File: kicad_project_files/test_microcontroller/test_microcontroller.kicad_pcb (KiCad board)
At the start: 2 copper layers, 60 x 100 mm, 40 parts, among them J1 USB_C_Receptacle_USB2.0, SW1 SW_Push, SW2 SW_Push, SW3 SW_Push, SW4 SW_Push, SW5 SW_Push, SW6 SW_Push, SW7 SW_Push, SW8 SW_Push, SW9 SW_Push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

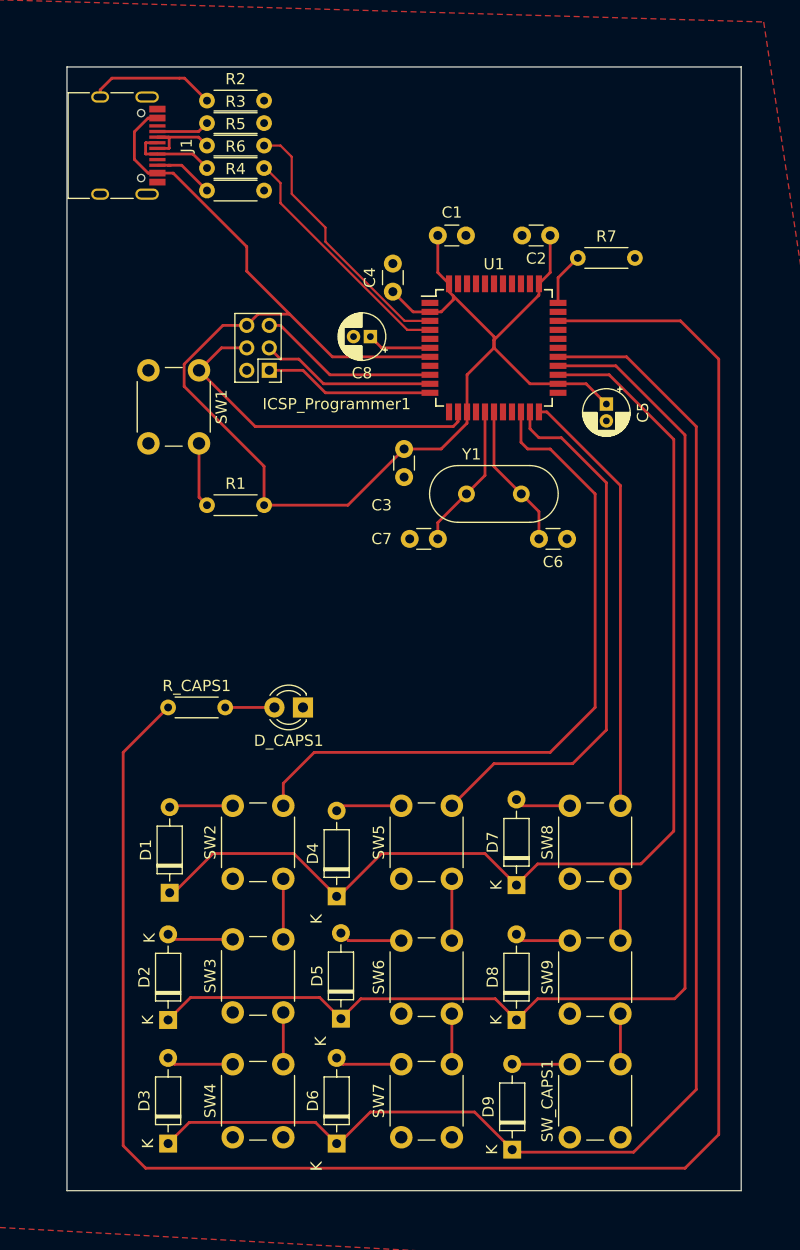
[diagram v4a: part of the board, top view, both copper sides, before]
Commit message: make tracks larger
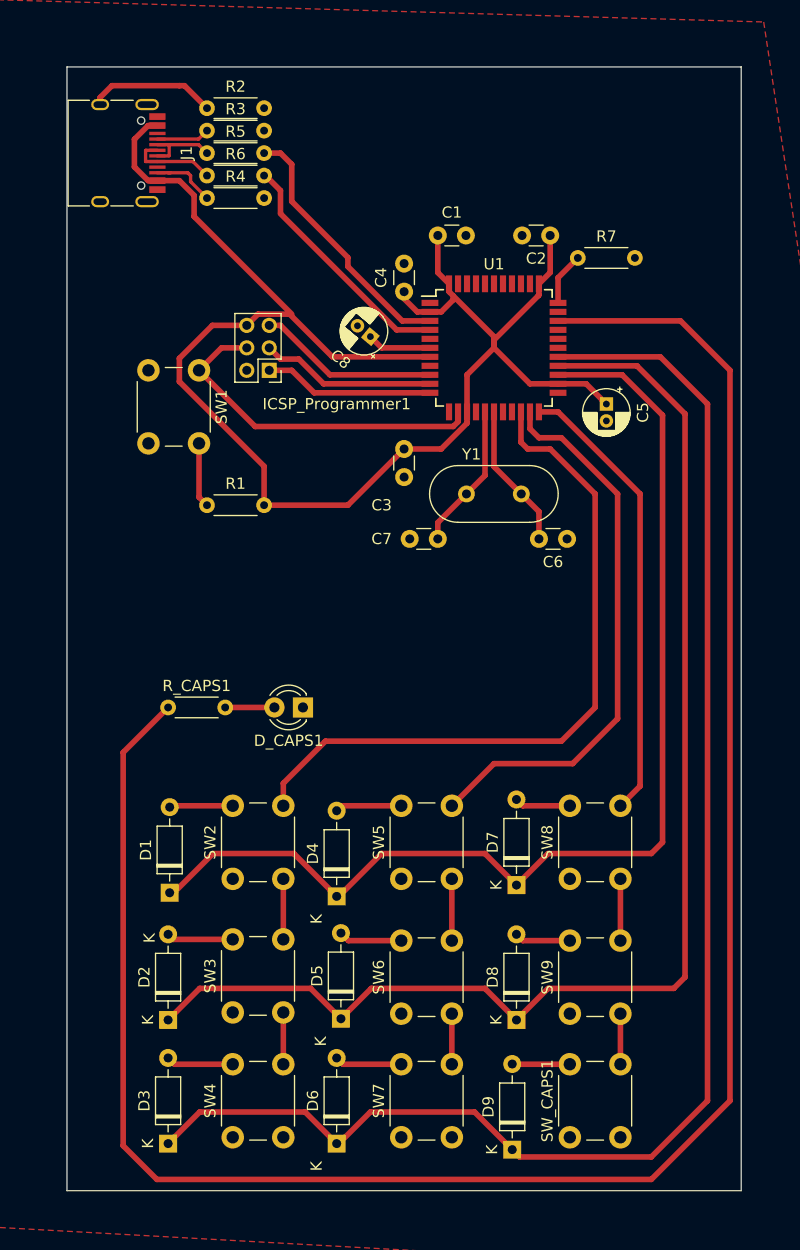
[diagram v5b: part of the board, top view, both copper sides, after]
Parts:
- moved C4 1.00 mm to (59.0, 40.0)
- moved J1 0.67 mm to (33.0, 27.7)
- moved R2 0.67 mm to (41.5, 23.7)
- moved R3 0.67 mm to (41.5, 25.7)
- moved R4 0.67 mm to (41.5, 31.7)
- moved R5 0.67 mm to (41.5, 27.7)
- moved R6 0.67 mm to (41.5, 29.7)
- turned C8 to 140 degrees
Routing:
- net ROW3: track 127.4 -> 132.3 mm
- net COL3: track 48.5 -> 50.5 mm
- net ROW2: track 113.4 -> 115.3 mm
- net COL2: track 58.8 -> 59.7 mm
- net D-: track 23.9 -> 23.3 mm

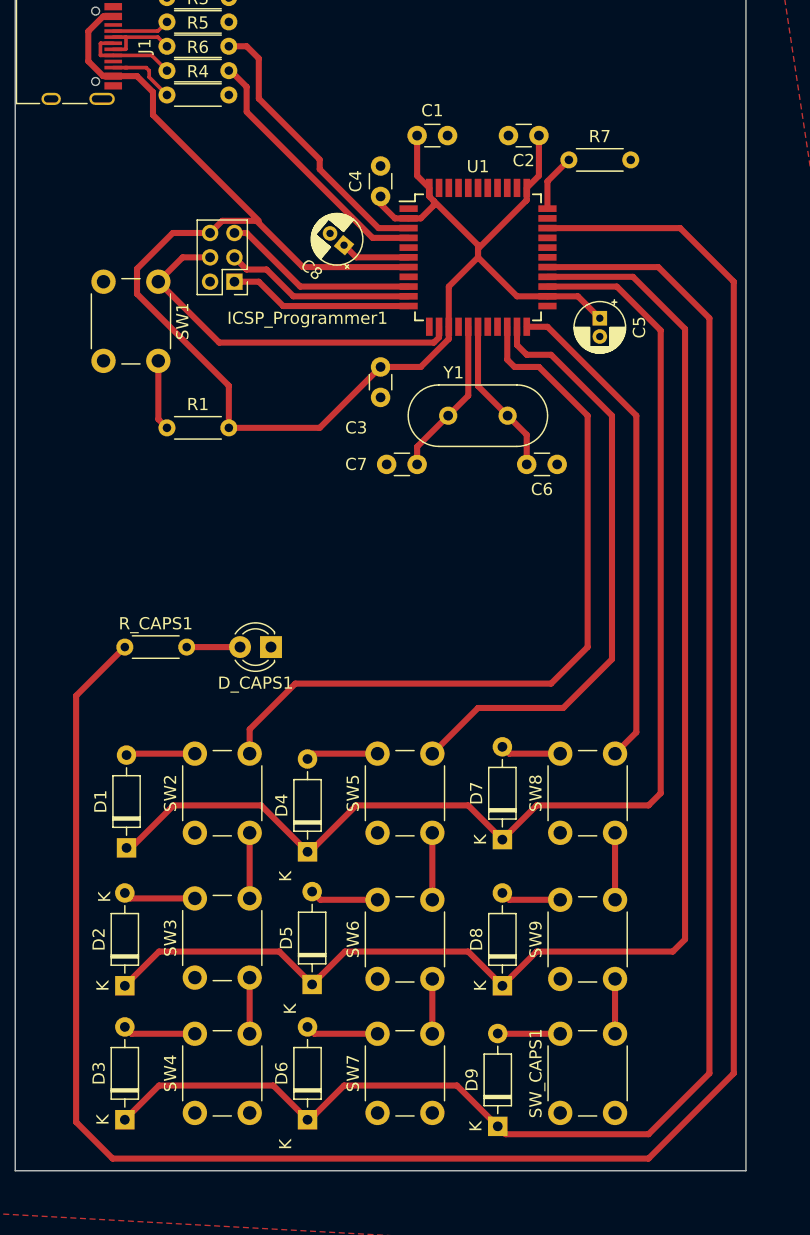
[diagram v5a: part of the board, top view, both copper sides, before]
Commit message: refactor pcb and export
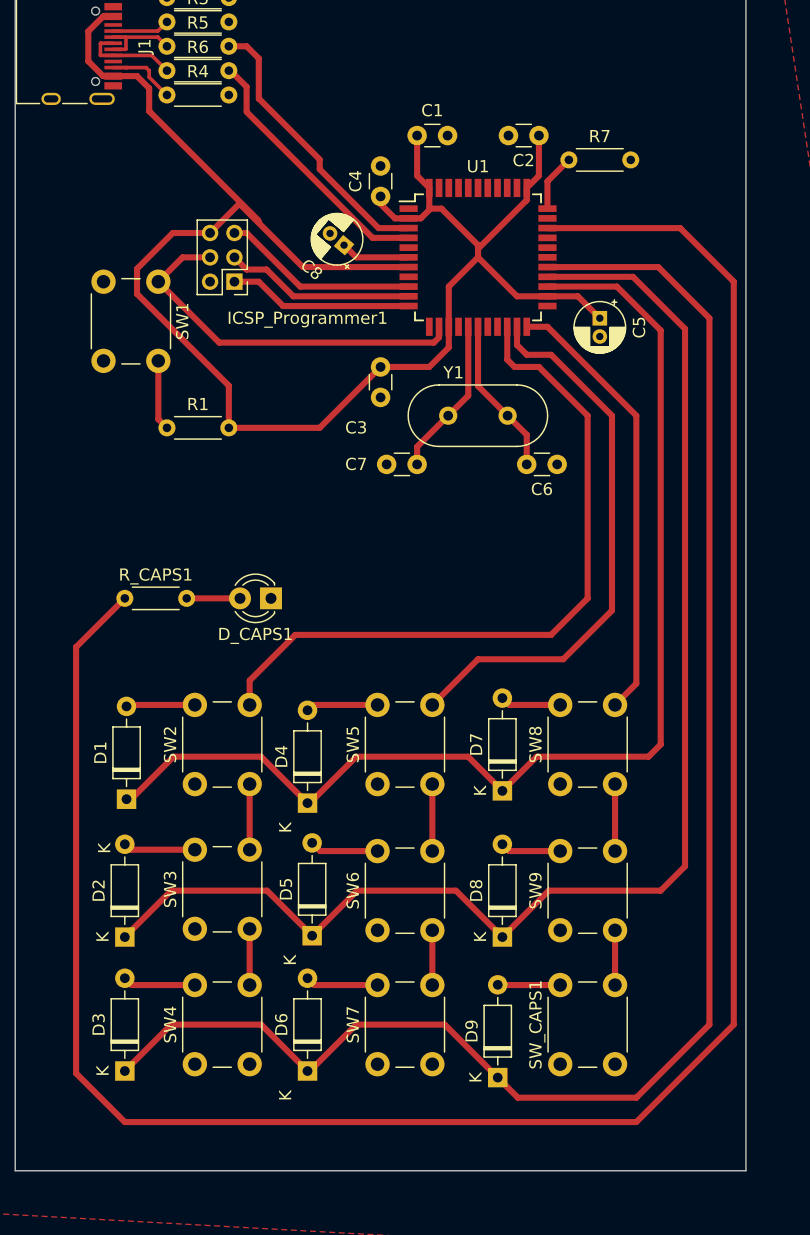
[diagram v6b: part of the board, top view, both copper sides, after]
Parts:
- moved D1 4.00 mm to (38.1, 89.5)
- moved D2 4.00 mm to (38.0, 100.8)
- moved D3 4.00 mm to (38.0, 111.8)
- moved D4 4.00 mm to (53.0, 89.8)
- moved D5 4.00 mm to (53.4, 100.7)
- moved D6 4.00 mm to (53.0, 111.8)
- moved D7 4.00 mm to (69.0, 88.8)
- moved D8 4.00 mm to (69.0, 100.8)
- moved D9 4.00 mm to (68.6, 112.3)
- moved D_CAPS1 4.00 mm to (50.0, 73.0)
- moved R_CAPS1 4.00 mm to (38.0, 73.0)
- moved SW2 4.00 mm to (43.8, 88.2)
- moved SW3 4.00 mm to (43.8, 100.1)
- moved SW4 4.00 mm to (43.8, 111.2)
- moved SW5 4.00 mm to (58.8, 88.2)
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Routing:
- net COL3: track 50.5 -> 46.5 mm
- net COL2: track 59.7 -> 55.7 mm
- net COL1: track 72.8 -> 68.8 mm
- net ROW1: track 100.0 -> 96.0 mm
- net ROW2: track 115.3 -> 111.8 mm
- net CAPS: track 180.9 -> 177.7 mm
- net ROW3: track 132.3 -> 130.7 mm
- net VCC: track 138.5 -> 139.9 mm
